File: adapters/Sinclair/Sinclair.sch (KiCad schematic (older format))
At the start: 2 parts, among them J1 JoyKEY, J2 Sinclair

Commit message: Tweaked sinclair adapter
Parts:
- J1: symbol c64_idc:C64_IDC2 -> c64_idc:C64_IDC_ADAPTER
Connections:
- net DOWN: now also J2.9; no longer J2.8
- net GND: now also J2.8
- no-connect marks 3 -> 4
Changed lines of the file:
@@
 $EndDescr
 $Comp
-L c64_idc:C64_IDC2 J1
+L c64_idc:C64_IDC_ADAPTER J1
 U 1 1 5FD1F19D
 P 4425 3000
@@
 Text Label 4850 4150 0    50   ~ 0
 UP
-Text Label 4850 4450 0    50   ~ 0
+Text Label 4850 4250 0    50   ~ 0
 DOWN
 $Comp
@@
 	6975 4750 7050 4750
 Wire Wire Line
-	7050 4450 4325 4450
+	4325 3450 4325 4250
 Wire Wire Line
-	4325 3450 4325 4450
+	7050 4250 4325 4250
+Wire Wire Line
+	6975 4750 6975 4450
+Wire Wire Line
+	6975 4450 7050 4450
+Connection ~ 6975 4750
+NoConn ~ 4625 2525
 $EndSCHEMATC

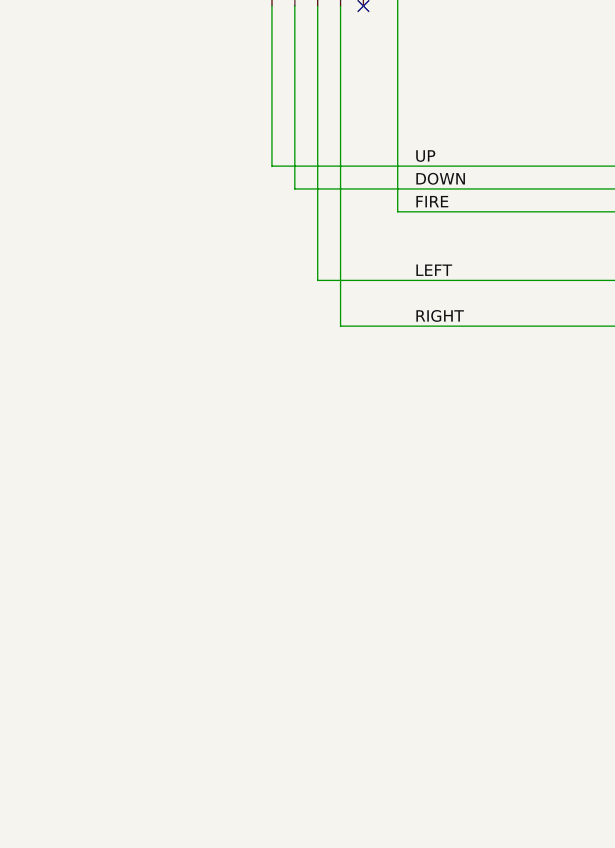
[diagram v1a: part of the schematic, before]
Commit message: Added male side to sinclair adapter
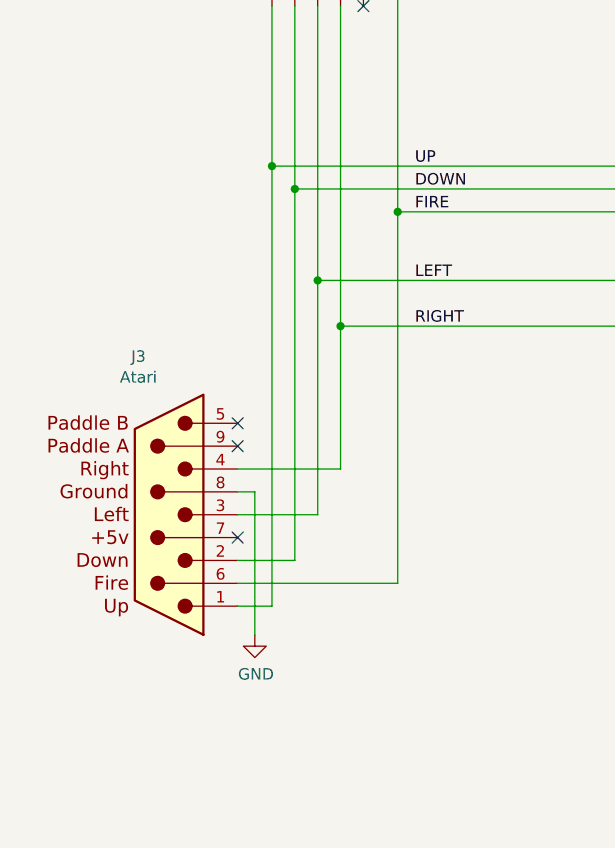
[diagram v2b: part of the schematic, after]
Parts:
- added J3: Atari, RND_DSUB:DSUB-9_Male_Edge, symbol atari_joystick:Atari_Port
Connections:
- net DOWN: now also J3.2
- net FIRE: now also J3.6
- net GND: now also J3.8 (GND)
- net LEFT: now also J3.3
- net RIGHT: now also J3.4
- net UP: now also J3.1
- no-connect marks 4 -> 7
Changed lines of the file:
@@
 Connection ~ 6975 4750
 NoConn ~ 4625 2525
+$Comp
+L atari_joystick:Atari_Port J3
+U 1 1 60303164
+P 3775 5675
+F 0 "J3" H 3909 6367 50  0000 C CNN
+F 1 "Atari" H 3909 6276 50  0000 C CNN
+F 2 "RND_DSUB:DSUB-9_Male_Edge" H 3775 5675 50  0001 C CNN
+F 3 "" H 3775 5675 50  0001 C CNN
+	1    3775 5675
+	-1   0    0    -1
+$EndComp
+$Comp
+L power:GND #PWR0101
+U 1 1 6030695F
+P 4150 6200
+F 0 "#PWR0101" H 4150 5950 50  0001 C CNN
+F 1 "GND" H 4155 6027 50  0000 C CNN
+F 2 "" H 4150 6200 50  0001 C CNN
+F 3 "" H 4150 6200 50  0001 C CNN
+	1    4150 6200
+	1    0    0    -1
+$EndComp
+Wire Wire Line
+	4075 5575 4150 5575
+Wire Wire Line
+	4150 5575 4150 6200
+NoConn ~ 4075 5275
+NoConn ~ 4075 5375
+NoConn ~ 4075 5775
+Wire Wire Line
+	4225 4150 4225 6075
+Connection ~ 4225 4150
+Wire Wire Line
+	4075 6075 4225 6075
+Wire Wire Line
+	4325 4250 4325 5875
+Wire Wire Line
+	4325 5875 4075 5875
+Connection ~ 4325 4250
+Wire Wire Line
+	4425 4650 4425 5675
+Wire Wire Line
+	4425 5675 4075 5675
+Connection ~ 4425 4650
+Wire Wire Line
+	4525 4850 4525 5475
+Wire Wire Line
+	4525 5475 4075 5475
+Connection ~ 4525 4850
+Connection ~ 4775 4350
+Wire Wire Line
+	4775 4350 4775 5975
+Wire Wire Line
+	4075 5975 4775 5975
 $EndSCHEMATC

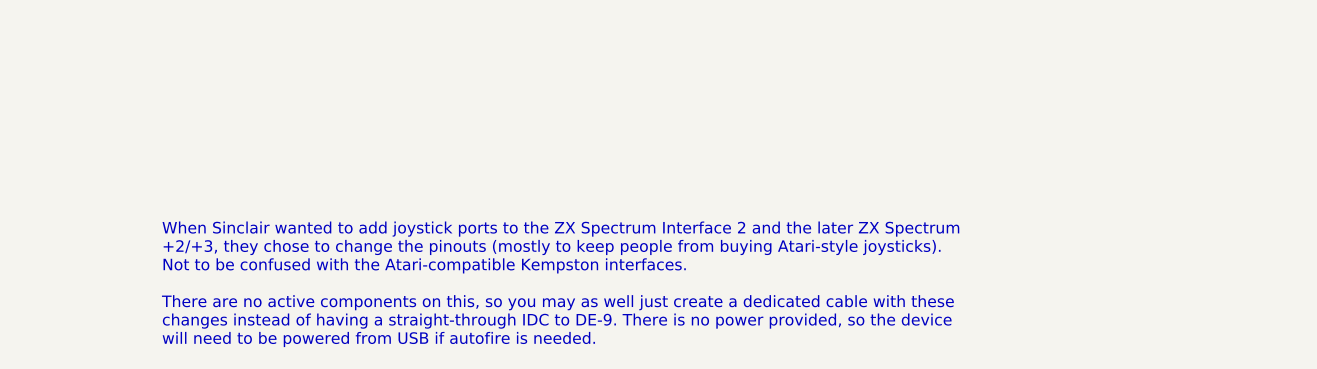
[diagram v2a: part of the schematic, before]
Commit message: Changed Sinclair adapter description
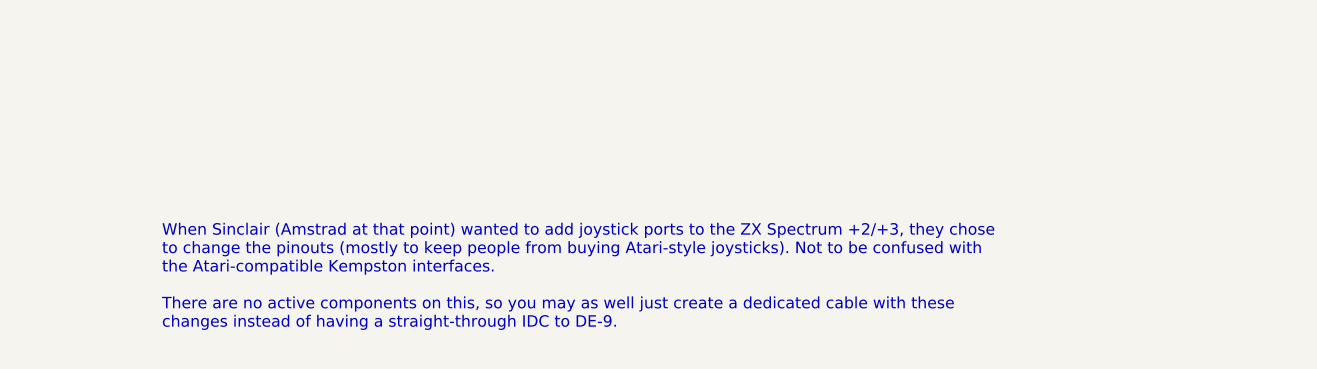
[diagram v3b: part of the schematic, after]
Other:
- note added: "When Sinclair (Amstrad at that point) wanted to add joystick ports to the ZX Spectrum +2/+3, they chose\nto change the pinouts (mostly to keep people from buying Atari-style joysticks). Not to be confused with\nthe Atari-compatible Kempston interfaces.\n\nThere are no active components on this, so you may as well just create a dedicated cable with these\nchanges instead of having a straight-throu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"
- note removed: "When Sinclair wanted to add joystick ports to the ZX Spectrum Interface 2 and the later ZX Spectrum\n+2/+3, they chose to change the pinouts (mostly to keep people from buying Atari-style joysticks). \nNot to be confused with the Atari-compatible Kempston interfaces.\n\nThere are no active components on this, so you may as well just create a dedicated cable with these\nchanges instead of having a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"
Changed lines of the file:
@@
 Wire Wire Line
 	4225 2050 4225 2525
-Text Notes 7000 7125 0    50   ~ 0
-When Sinclair wanted to add joystick ports to the ZX Spectrum Interface 2 and the later ZX Spectrum\n+2/+3, they chose to change the pinouts (mostly to keep people from buying Atari-style joysticks). \nNot to be confused with the Atari-compatible Kempston interfaces.\n\nThere are no active components on this, so you may as well just create a dedicated cable with these\nchanges instead of having a straight-through IDC to DE-9. There is no power provided, so the device\nwill need to be powered from USB if autofire is needed.
+Text Notes 7000 7050 0    50   ~ 0
+When Sinclair (Amstrad at that point) wanted to add joystick ports to the ZX Spectrum +2/+3, they chose\nto change the pinouts (mostly to keep people from buying Atari-style joysticks). Not to be confused with\nthe Atari-compatible Kempston interfaces.\n\nThere are no active components on this, so you may as well just create a dedicated cable with these\nchanges instead of having a straight-through IDC to DE-9.
 $Comp
 L joykey_jumpers:JUMPER_SETTINGS_1 #1
